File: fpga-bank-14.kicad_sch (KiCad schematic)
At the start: 20 parts, among them U4 XC7K160T-FFG676

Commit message: Finish reconnecting signals after migration to the hierarchical structure
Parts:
- gave numbers to parts that had none: 15
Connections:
- net AUX_JTAG_RST is gone; now on net AUX.RST: U4.G25 (IO_L16P_T2_CSI_B_14)
- net AUX_JTAG_TCK is gone; now on net AUX.TCK: U4.C24 (IO_L6N_T0_D08_VREF_14)
- net AUX_JTAG_TDI is gone; now on net AUX.TDI: U4.D24 (IO_L11N_T1_SRCC_14)
- net AUX_JTAG_TDO is gone; now on net AUX.TDO: U4.C26 (IO_L5N_T0_D07_14)
- net AUX_JTAG_TMS is gone; now on net AUX.TMS: U4.D25 (IO_L15N_T2_DQS_DOUT_CSO_B_14)
- net FCS_B is gone; now on net FLASH.~{CS}: U4.C23 (IO_L6P_T0_FCS_B_14)
- net QSPI_DQ0 is gone; now on net FLASH.IO0: U4.B24 (IO_L1P_T0_D00_MOSI_14)
- net QSPI_DQ1 is gone; now on net FLASH.IO1: U4.A25 (IO_L1N_T0_D01_DIN_14)
- net QSPI_DQ2 is gone; now on net FLASH.IO2: U4.B22 (IO_L2P_T0_D02_14)
- net QSPI_DQ3 is gone; now on net FLASH.IO3: U4.A22 (IO_L2N_T0_D03_14)
- net SCL_3V3 is gone; now on net FPGA_DDR.SCL: U4.E25 (IO_L15P_T2_DQS_RDWR_B_14)
- net SDA_3V3 is gone; now on net FPGA_DDR.SDA: U4.D26 (IO_L5P_T0_D06_14)
- net UART0_RX is gone; now on net UART0.RX: U4.F25 (IO_L17P_T2_A14_D30_14)
- net UART0_TX is gone; now on net UART0.TX: U4.E26 (IO_L17N_T2_A13_D29_14)
- net UART1_RX is gone; now on net UART1.RX: U4.A24 (IO_L4N_T0_D05_14)
- net UART1_TX is gone; now on net UART1.TX: U4.A23 (IO_L4P_T0_D04_14)
- net CLK_DIR: no longer names the net of U4.F24 (IO_L14N_T2_SRCC_14)
- net PRSNT_M2C: no longer names the net of U4.E23 (IO_L12N_T1_MRCC_14)
- net PWR_SCL_3V3 renamed FPGA_PWR.SCL
- net PWR_SDA_3V3 renamed FPGA_PWR.SDA
- no-connect marks 16 -> 18
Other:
- note added: "CLK_DIR"
- note added: "PRSNT_M2C"
- moved on the sheet: U4C

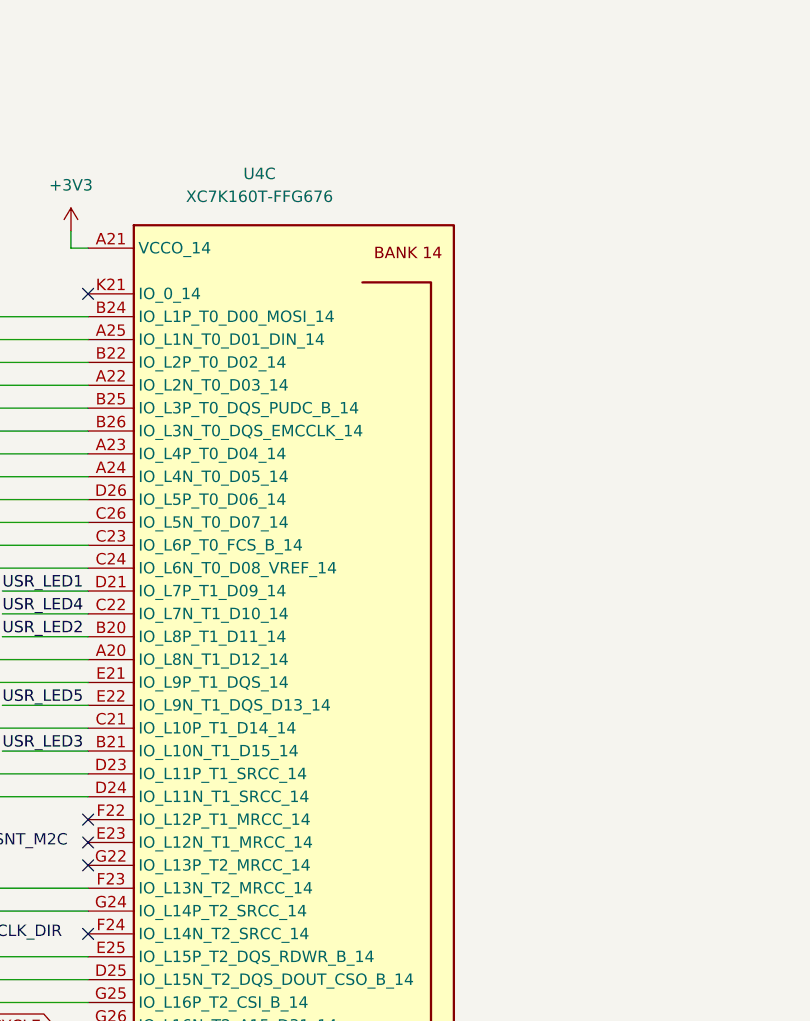
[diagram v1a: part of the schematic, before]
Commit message: Fix FPGA properties from the standardized library, update SO-DIMM symbol
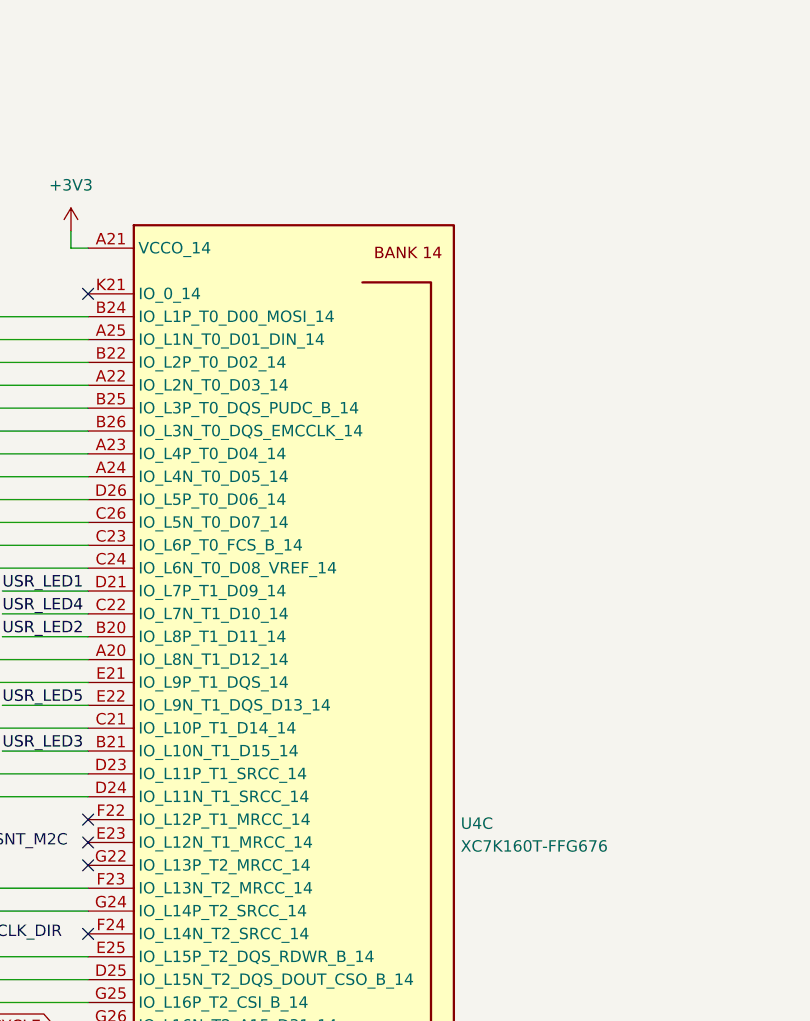
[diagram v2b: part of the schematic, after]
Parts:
- U4: footprint sodimm-ddr5-tester-footprints:BGA-676_27x27mm_Layout26x26_P1X1mm -> antmicro-footprints:BGA-676_27x27mm_Layout26x26_P1X1mm; symbol sodimm-ddr5-tester:XC7K160T-FFG676 -> antmicroMicrocontrollers:XC7K160T-FFG676; Manufacturer Xilinx -> AMD-Xilinx
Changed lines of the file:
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@@
     (pin "1")
   )
-  (symbol (lib_id "sodimm-ddr5-tester:XC7K160T-FFG676") (at 195.58 70.485 0) (unit 3)
+  (symbol (lib_id "antmicroMicrocontrollers:XC7K160T-FFG676") (at 195.58 70.485 0) (unit 3)
     (in_bom yes) (on_board yes) (fields_autoplaced)
-    (property "Reference" "U4" (id 0) (at 214.63 62.23 0))
-    (property "Value" "XC7K160T-FFG676" (id 1) (at 214.63 64.77 0)
-      (effects (font (size 1.27 1.27) (thickness 0.15)))
+    (property "Reference" "U4" (id 0) (at 236.982 134.4244 0)
+      (effects (font (size 1.27 1.27)) (justify left))
     )
-    (property "Footprint" "sodimm-ddr5-tester-footprints:BGA-676_27x27mm_Layout26x26_P1X1mm" (id 2) (at 264.16 73.025 0)
+    (property "Value" "XC7K160T-FFG676" (id 1) (at 236.982 136.9547 0)
+      (effects (font (size 1.27 1.27) (thickness 0.15)) (justify left))
+    )
+    (property "Footprint" "antmicro-footprints:BGA-676_27x27mm_Layout26x26_P1X1mm" (id 2) (at 264.16 73.025 0)
       (effects (font (size 1.27 1.27) (thickness 0.15)) (justify left bottom) hide)
     )
@@
       (effects (font (size 1.27 1.27) (thickness 0.15)) (justify left bottom) hide)
     )
-    (property "Manufacturer" "Xilinx" (id 7) (at 195.58 70.485 0)
+    (property "Manufacturer" "AMD-Xilinx" (id 7) (at 195.58 70.485 0)
       (effects (font (size 1.27 1.27)) hide)
     )

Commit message: Loclib of the project
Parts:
- U4: footprint antmicro-footprints:BGA-676_27x27mm_Layout26x26_P1X1mm -> sodimm-ddr5-tester-footprints:BGA-676_27x27mm_Layout26x26_P1X1mm; symbol antmicroMicrocontrollers:XC7K160T-FFG676 -> sodimm-ddr5-tester:XC7K160T-FFG676

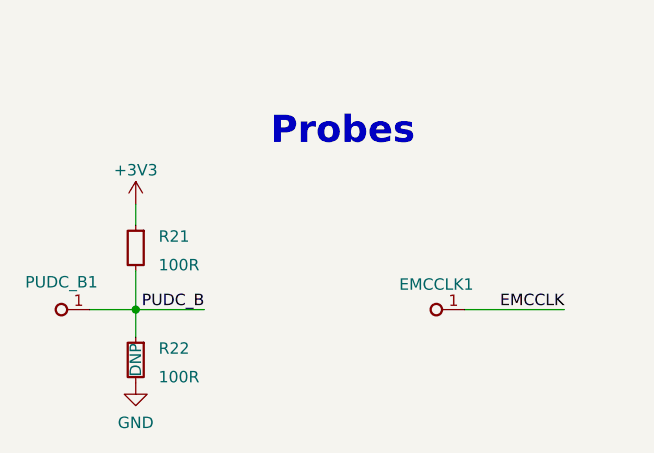
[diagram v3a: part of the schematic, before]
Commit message: Finish updating components to newest versions, improve silkscreen marking, bump revision
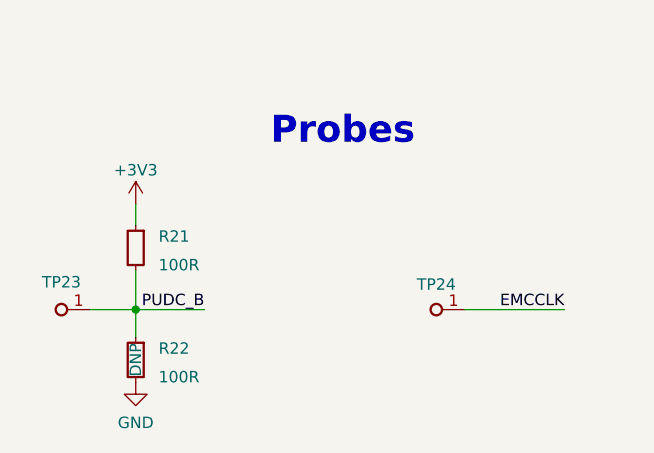
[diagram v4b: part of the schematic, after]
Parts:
- renumbered PUDC_B1 to TP23, EMCCLK1 to TP24
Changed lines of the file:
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@@
     (title_block
         (title "SO-DIMM DDR5 Tester")
-        (date "2024-01-10")
-        (rev "1.1.0")
+        (date "2024-01-18")
+        (rev "1.1.1")
         (comment 1 "www.antmicro.com")
         (comment 2 "Antmicro Ltd"))
@@
         (on_board yes)
         (fields_autoplaced)
-        (property "Reference" "EMCCLK1"
+        (property "Reference" "TP24"
             (id 0)
             (at 124.841 237.871 0))
@@
         (on_board yes)
         (fields_autoplaced)
-        (property "Reference" "PUDC_B1"
+        (property "Reference" "TP23"
             (id 0)
             (at 83.185 237.617 0))

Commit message: Finish schematic cleanup
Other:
- moved on the sheet: D4, D5, D6, D7, D8, Q4, Q5, Q6, Q7, Q8, R21, R22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

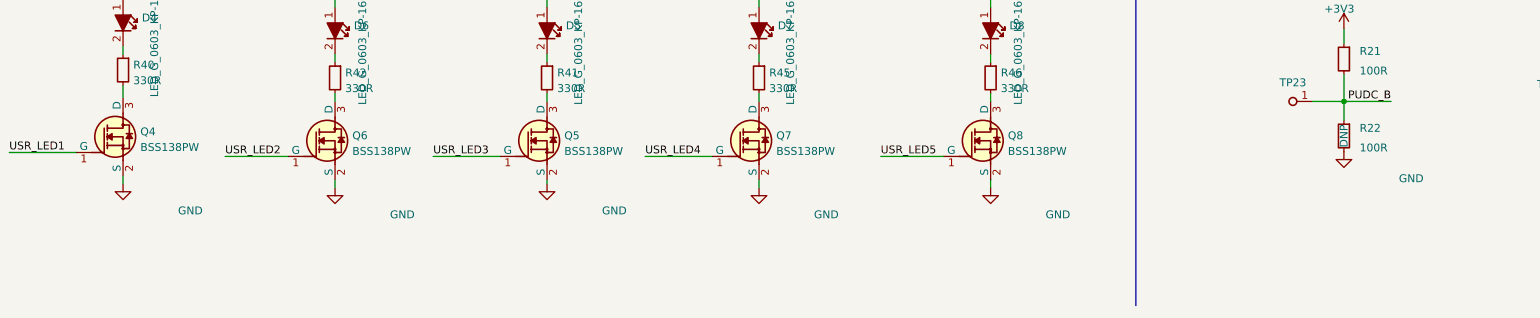
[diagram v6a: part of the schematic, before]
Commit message: Add updated components to local library
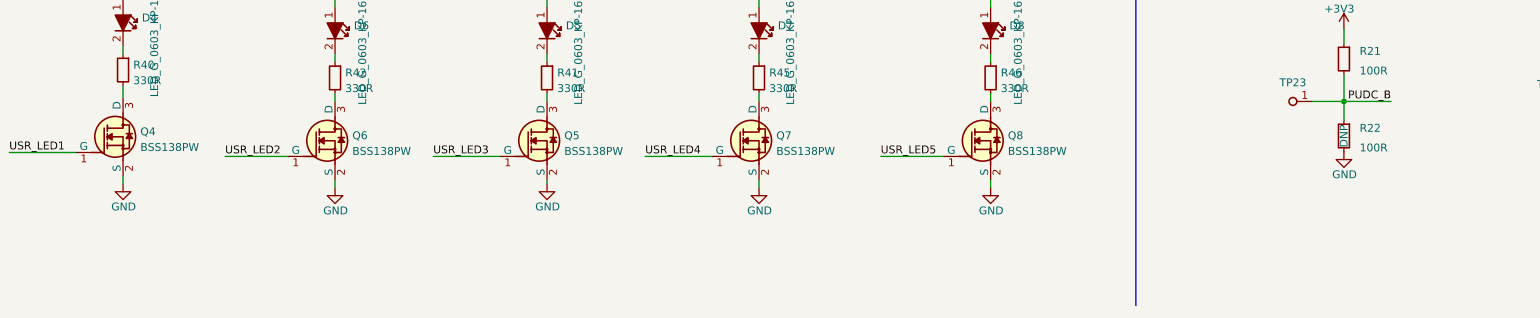
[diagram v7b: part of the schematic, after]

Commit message: [#57478] ohp release
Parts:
- D4, D5, D6, D7, D8: footprint sodimm-ddr5-tester-footprints:LED_0603_1608Metric_G -> antmicro-footprints:LED_0603_1608Metric_G; symbol sodimm-ddr5-tester:LED_G_0603_KP-1608CGCK -> antmicroLEDIndicationDiscrete:LED_G_0603_KP-1608CGCK
- Q4, Q5, Q6, Q7, Q8: footprint sodimm-ddr5-tester-footprints:SC70-3 -> antmicro-footprints:SC70-3; symbol sodimm-ddr5-tester:BSS138PW -> antmicroTransistorsFETsMOSFETsSingle:BSS138PW
- R21: footprint sodimm-ddr5-tester-footprints:R_0402_1005Metric -> antmicro-footprints:R_0402_1005Metric; symbol sodimm-ddr5-tester:R_100R_0402 -> antmicroResistors0402:R_100R_0402
- R22: footprint sodimm-ddr5-tester-footprints:R_0402_1005Metric -> antmicro-footprints:R_0402_1005Metric; symbol sodimm-ddr5-tester:R_100R_0402 -> antmicroResistors0402:R_100R_0402; now not fitted; now left out of the parts list
- R40, R41, R42, R45, R46: footprint sodimm-ddr5-tester-footprints:R_0402_1005Metric -> antmicro-footprints:R_0402_1005Metric; symbol sodimm-ddr5-tester:R_330R_0402 -> antmicroResistors0402:R_330R_0402
- TP23, TP24: footprint sodimm-ddr5-tester-footprints:TP_SMD_1mm -> antmicro-footprints:TP_SMD_1mm; symbol sodimm-ddr5-tester:TP_1mm_SMD -> antmicroTestPoints:TP_1mm_SMD
- U4: footprint sodimm-ddr5-tester-footprints:BGA-676_27x27mm_Layout26x26_P1X1mm -> antmicro-footprints:BGA-676_27x27mm_Layout26x26_P1x1mm_FFG676; symbol sodimm-ddr5-tester:XC7K160T-FFG676 -> antmicroFPGAChips:XC7K160T-FFG676
